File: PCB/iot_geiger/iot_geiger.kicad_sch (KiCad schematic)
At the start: 63 parts, among them J1 Program, J2 Display, J3 IO, J4 5V DC, J5 PM, Q1 PBHV8540Z, Q2 BC817, SW1 SW_Update, U1 NINA-W102, U2 AM2302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

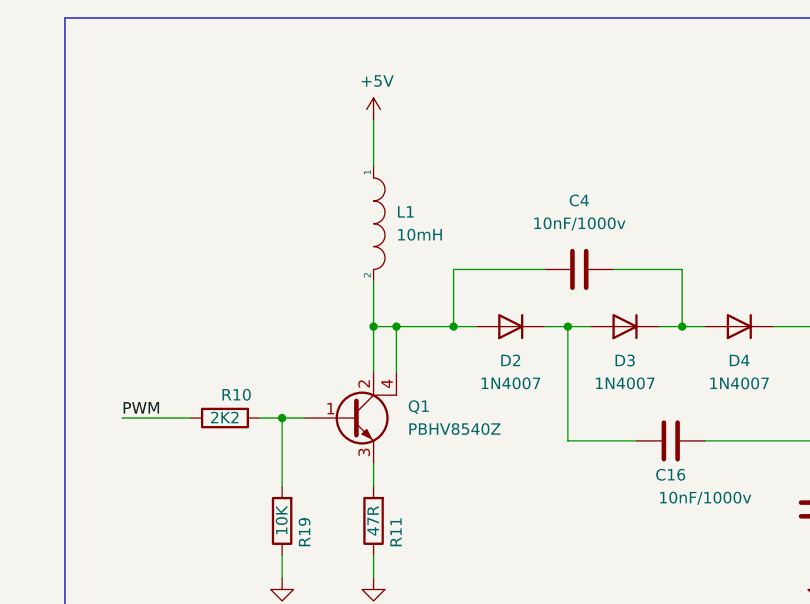
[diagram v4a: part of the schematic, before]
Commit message: add webserver
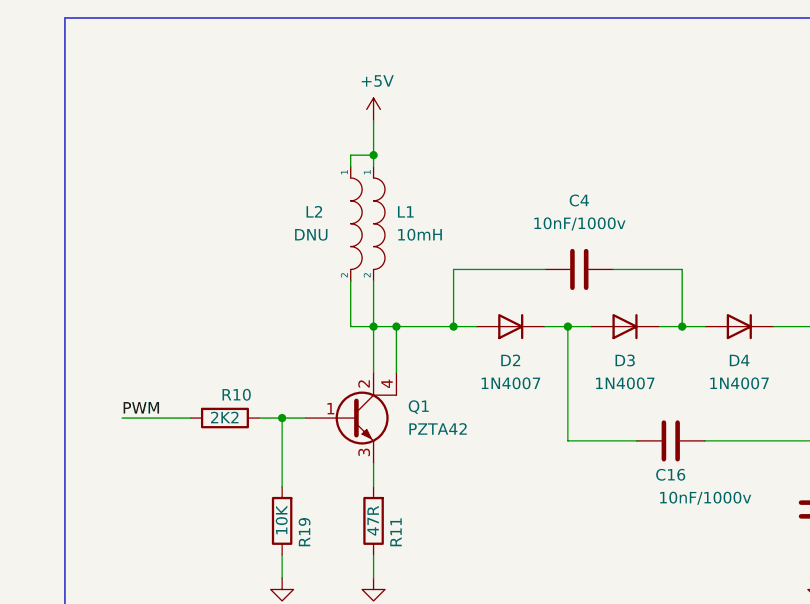
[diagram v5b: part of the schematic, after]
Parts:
- added L2: DNU, Inductor_THT:L_Radial_D10.0mm_P5.00mm_Fastron_07M, symbol pspice:INDUCTOR
- Q1: value PBHV8540Z -> PZTA42
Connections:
- net +5V: now also L2.1
- net at C4.1, D2.2 (A), L1.2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: now also L2.2
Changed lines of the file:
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@@
   (junction (at 182.88 73.66) (diameter 0) (color 0 0 0 0)
   )
+  (junction (at 120.65 41.91) (diameter 0) (color 0 0 0 0)
+  )
   (junction (at 147.32 256.54) (diameter 0) (color 0 0 0 0)
   )
@@
     (stroke (width 0) (type default) (color 0 0 0 0))
   )
+  (wire (pts (xy 118.11 60.96) (xy 120.65 60.96))
+    (stroke (width 0) (type default) (color 0 0 0 0))
+  )
   (wire (pts (xy 219.71 73.66) (xy 219.71 76.2))
     (stroke (width 0) (type default) (color 0 0 0 0))
@@
     (stroke (width 0) (type default) (color 0 0 0 0))
   )
-  (wire (pts (xy 120.65 38.1) (xy 120.65 43.18))
+  (wire (pts (xy 120.65 38.1) (xy 120.65 41.91))
     (stroke (width 0) (type default) (color 0 0 0 0))
   )
@@
     (stroke (width 0) (type default) (color 0 0 0 0))
   )
+  (wire (pts (xy 118.11 41.91) (xy 120.65 41.91))
+    (stroke (width 0) (type default) (color 0 0 0 0))
+  )
   (wire (pts (xy 251.46 201.93) (xy 251.46 203.2))
     (stroke (width 0) (type default) (color 0 0 0 0))
@@
     (stroke (width 0) (type default) (color 0 0 0 0))
   )
+  (wire (pts (xy 118.11 43.18) (xy 118.11 41.91))
+    (stroke (width 0) (type default) (color 0 0 0 0))
+  )
   (wire (pts (xy 127 184.15) (xy 127 189.23))
     (stroke (width 0) (type default) (color 0 0 0 0))
@@
     (stroke (width 0) (type default) (color 0 0 0 0))
   )
+  (wire (pts (xy 120.65 41.91) (xy 120.65 43.18))
+    (stroke (width 0) (type default) (color 0 0 0 0))
+  )
   (wire (pts (xy 182.88 86.36) (xy 198.12 86.36))
     (stroke (width 0) (type default) (color 0 0 0 0))
@@
   )
   (wire (pts (xy 157.48 156.21) (xy 129.54 156.21))
+    (stroke (width 0) (type default) (color 0 0 0 0))
+  )
+  (wire (pts (xy 118.11 55.88) (xy 118.11 60.96))
     (stroke (width 0) (type default) (color 0 0 0 0))
   )
@@
       (effects (font (size 1.27 1.27)) (justify left))
     )
-    (property "Value" "PBHV8540Z" (id 1) (at 124.46 72.3899 0)
+    (property "Value" "PZTA42" (id 1) (at 124.46 72.3899 0)
       (effects (font (size 1.27 1.27)) (justify left))
     )
@@
     )
   )
+  (symbol (lib_id "pspice:INDUCTOR") (at 118.11 49.53 270) (unit 1)
+    (in_bom yes) (on_board yes)
+    (property "Reference" "L2" (id 0) (at 113.03 48.26 90)
+      (effects (font (size 1.27 1.27)) (justify left))
+    )
+    (property "Value" "DNU" (id 1) (at 111.76 50.8 90)
+      (effects (font (size 1.27 1.27)) (justify left))
+    )
+    (property "Footprint" "Inductor_THT:L_Radial_D10.0mm_P5.00mm_Fastron_07M" (id 2) (at 118.11 49.53 0)
+      (effects (font (size 1.27 1.27)) hide)
+    )
+    (property "Datasheet" "~" (id 3) (at 118.11 49.53 0)
+      (effects (font (size 1.27 1.27)) hide)
+    )
+    (pin "1")
+    (pin "2")
+  )
   (symbol (lib_id "power:+3.3V") (at 298.45 41.91 0) (unit 1)
     (in_bom yes) (on_board yes) (fields_autoplaced)
@@
       (reference "L1") (unit 1) (value "10mH") (footprint "Inductor_SMD:L_12x12mm_H6mm")
     )
+    (path "/bb2ca589-2eb0-4335-b970-182fc6526d12"
+      (reference "L2") (unit 1) (value "DNU") (footprint "Inductor_THT:L_Radial_D10.0mm_P5.00mm_Fastron_07M")
+    )
     (path "/6d3fe2e2-f863-41e5-8e0c-e75fee38bb03"
-      (reference "Q1") (unit 1) (value "PBHV8540Z") (footprint "Package_TO_SOT_SMD:SOT-223")
+      (reference "Q1") (unit 1) (value "PZTA42") (footprint "Package_TO_SOT_SMD:SOT-223")
     )
     (path "/3ce191a3-9985-4bc7-98f2-9cbe9be43819"
